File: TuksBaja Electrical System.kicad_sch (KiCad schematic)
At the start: 16 parts, among them U1 LM358, U2 A1104xLH, U3 ESP32-S3-WROOM-1, U4 A1104xLH, U5 LM358

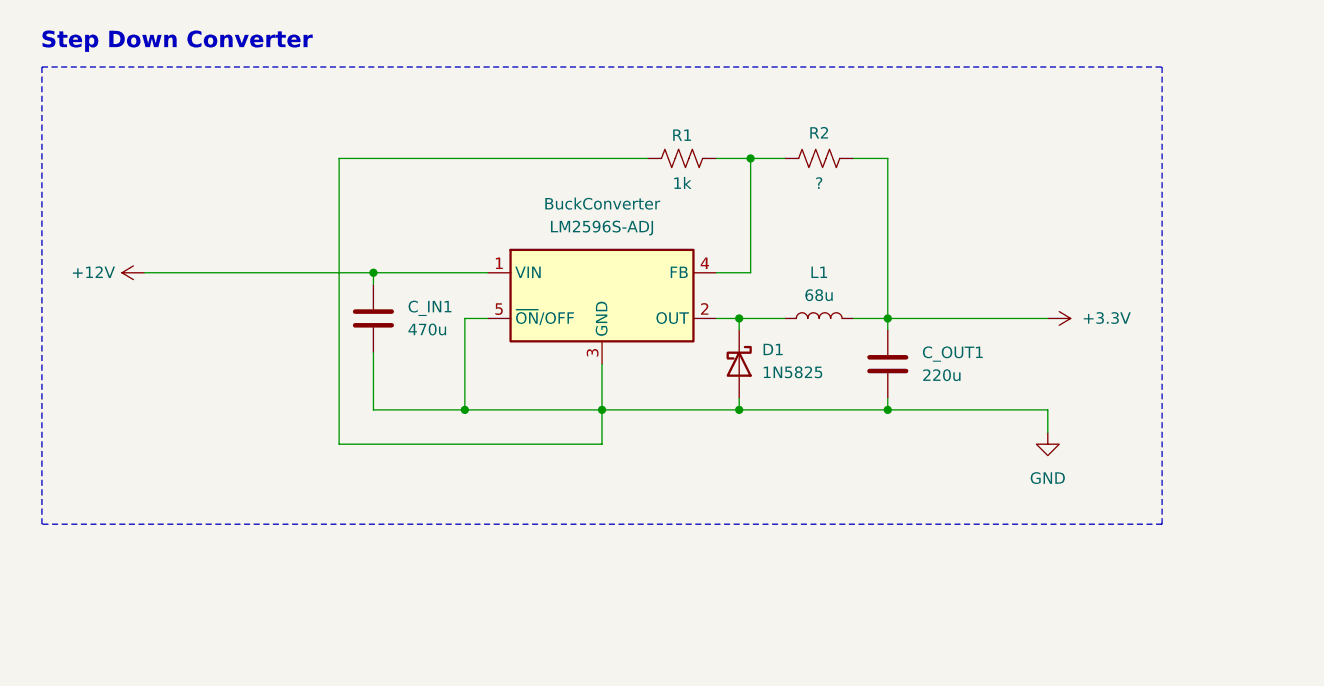
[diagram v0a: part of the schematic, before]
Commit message: added buck converter files
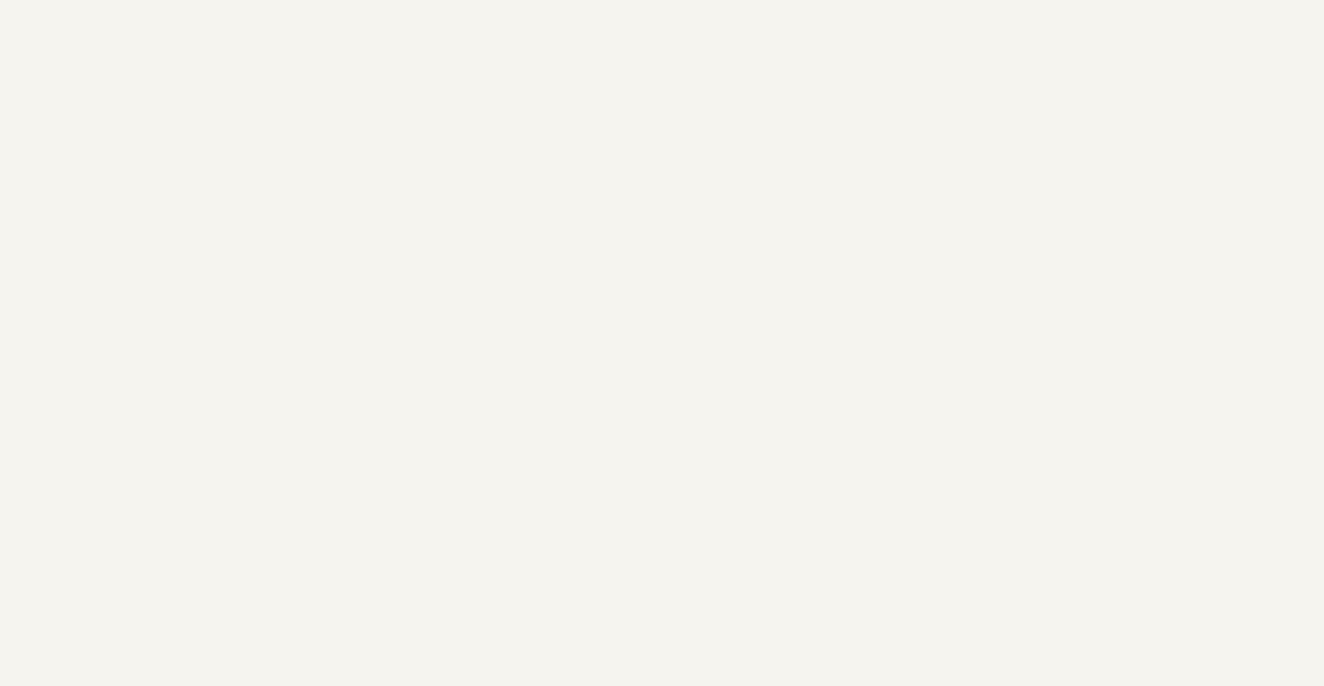
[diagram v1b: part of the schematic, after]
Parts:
- removed BuckConverter: LM2596S-ADJ, Package_TO_SOT_SMD:TO-263-5_TabPin3, symbol Regulator_Switching:LM2596S-ADJ
- removed C_IN1: 470u, symbol Device:C
- removed C_OUT1: 220u, symbol Device:C
- removed D1: 1N5825, symbol Device:D_Schottky
- removed L1: 68u, symbol Device:L
- removed R1: 1k, symbol Device:R_US
- removed R2: ?, symbol Device:R_US
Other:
- note removed: "Step Down Converter"

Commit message: Overhall Schematic
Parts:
- removed C1, C2: 0.1u, symbol Device:C
- removed R3, R4: 100k, symbol Device:R
- removed U1, U5: LM358, symbol Amplifier_Operational:LM358
- removed U2, U4: A1104xLH, Package_TO_SOT_SMD:SOT-23W, symbol Sensor_Magnetic:A1104xLH
- removed U3: ESP32-S3-WROOM-1, RF_Module:ESP32-S3-WROOM-1, symbol RF_Module:ESP32-S3-WROOM-1
- added BUCK_1, BUCK_2: MountingHole, symbol Mechanical:MountingHole
- added Battery_Terminal: Screw_Terminal_01x02, symbol Connector:Screw_Terminal_01x02
- added ESP_LEFT, ESP_RIGHT: Conn_01x15, symbol Connector_Generic:Conn_01x15
- added FL_WS, FR_WS, RL_WS, RR_WS: Conn_01x03, symbol Connector_Generic:Conn_01x03
- added IN_GND, OUT_GND, VIN, VOUT: Conn_01x01_Pin, symbol Connector:Conn_01x01_Pin
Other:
- note added: "ESP Mounting"
- note added: "Power Supply"
- note added: "Wheel Sensors"
- note removed: "0.1 uF capacitor for decoupling"
- note removed: "Rear Left Wheel Speed"
- note removed: "Rear Right Wheel Speed"
